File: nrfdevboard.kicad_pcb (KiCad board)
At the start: 4 copper layers, 26 x 26.2 mm, 17 parts, among them J1 Conn_01x07_Pin, J2 Conn_01x07_Pin, P1 USB_C_Plug_USB2.0, U1 MDBT50Q-P1MV2, U3 AP2112K-3.3TRG1, Y1 O_32.768kHz

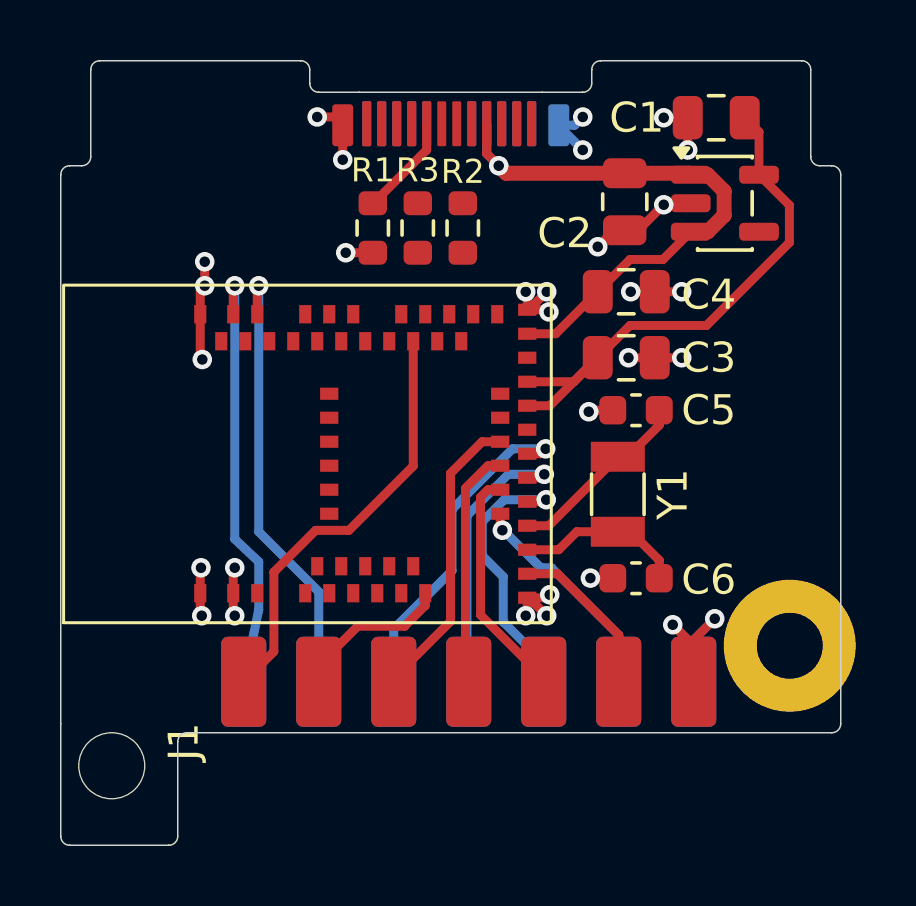
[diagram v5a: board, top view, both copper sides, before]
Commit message: Routing done (outside USB) + added some more pins
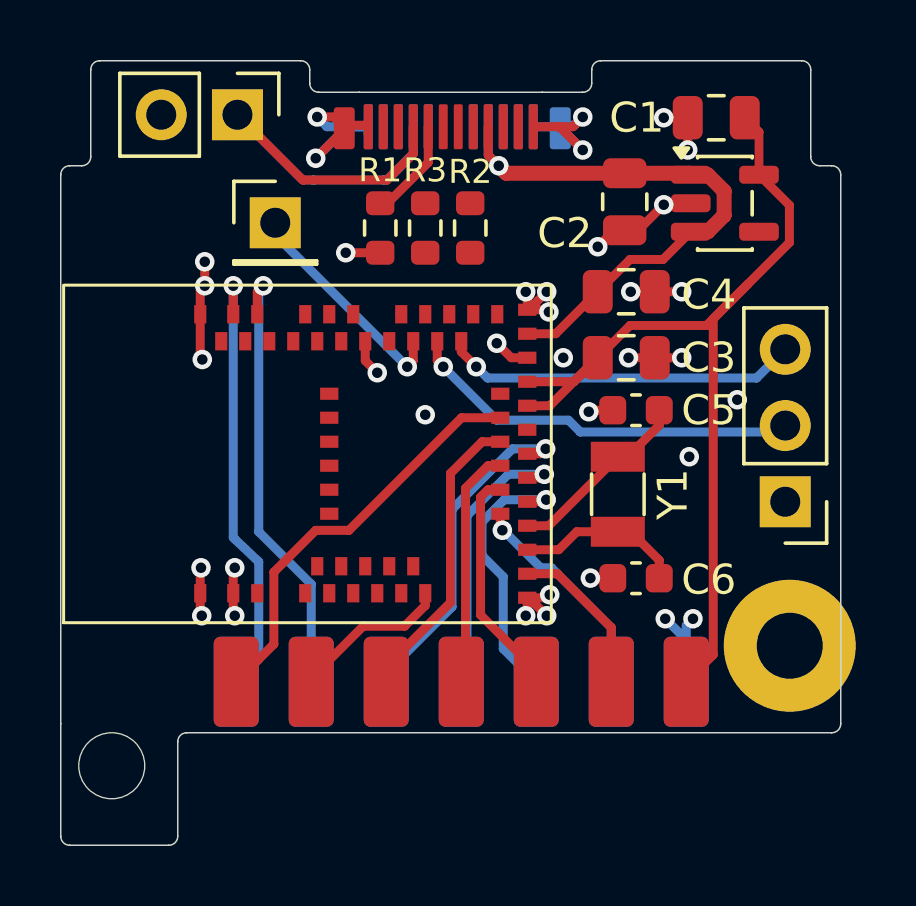
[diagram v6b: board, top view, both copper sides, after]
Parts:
- added J3: 3_tht_side, Connector_PinHeader_2.54mm:PinHeader_1x03_P2.54mm_Vertical, F.Cu at (107.2, 125.7)
- added J4: 2_tht_top, Connector_PinHeader_2.54mm:PinHeader_1x02_P2.54mm_Vertical, F.Cu at (88.9, 112.8)
- added J5: 1_tht_top, Connector_PinHeader_2.54mm:PinHeader_1x01_P2.54mm_Vertical, F.Cu at (90.2, 116.4)
- J1: value Conn_01x07_Pin -> 7_print_front
- J2: value Conn_01x07_Pin -> 7_pin_back
- P1: value USB_C_Plug_USB2.0 -> Straddle_USB_type_c; footprint TH-1-CC:USBC -> TH-1-CC_footprints:USBC
- moved J1 0.25 mm to (87.4, 133.7)
- moved J2 0.25 mm to (87.4, 129.7)
- moved R1 0.25 mm to (93.7, 116.6)
- moved R2 0.25 mm to (96.7, 116.6)
- moved R3 0.25 mm to (95.2, 116.6)
- moved P1 0.11 mm to (92.0, 112.5)
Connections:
- J1 pad 7: GND -> +3.3V
- P1 pad A10: (no net) -> unconnected-(P1-RX2--PadA10)
- P1 pad A11: (no net) -> unconnected-(P1-RX2+-PadA11)
- P1 pad A2: (no net) -> unconnected-(P1-TX1+-PadA2)
- P1 pad A3: (no net) -> unconnected-(P1-TX1--PadA3)
- P1 pad A8: (no net) -> unconnected-(P1-SBU1-PadA8)
- P1 pad B10: (no net) -> unconnected-(P1-RX1--PadB10)
- P1 pad B11: (no net) -> unconnected-(P1-RX1+-PadB11)
- P1 pad B2: (no net) -> unconnected-(P1-TX2+-PadB2)
- P1 pad B3: (no net) -> unconnected-(P1-TX2--PadB3)
- P1 pad B8: (no net) -> unconnected-(P1-SBU2-PadB8)
- U1 pad 27: unconnected-(U1A-P0.11/TRACEDATA2-Pad27) -> PIN8
- U1 pad 36: unconnected-(U1A-P0.14-Pad36) -> PIN15
- U1 pad 38: unconnected-(U1A-P0.16-Pad38) -> PIN16
- U1 pad 40: PIN8 -> PIN20
- U1 pad 43: unconnected-(U1A-P0.21-Pad43) -> PIN17
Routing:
- net PIN17: track 0.00 -> 16.6 mm, vias 0 -> 1
- net VBUS: track 20.0 -> 35.8 mm
- net +3.3V: track 18.5 -> 33.7 mm
- net PIN16: track 0.00 -> 13.3 mm, vias 0 -> 1
- net PIN15: track 0.00 -> 11.9 mm, vias 0 -> 1
- net PIN20: track 0.00 -> 7.56 mm, vias 0 -> 1
- net GND: track 36.1 -> 42.2 mm, vias 30 -> 34
- net unconnected-(U1B-DCCH-Pad31): track 0.00 -> 1.22 mm, vias 0 -> 1
- net PIN9: track 5.33 -> 5.88 mm
- net PIN5: track 9.29 -> 9.83 mm
- added copper zone on In2.Cu, net GND

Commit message: Basics done. Will need to optimise double check DFM before manufacturing
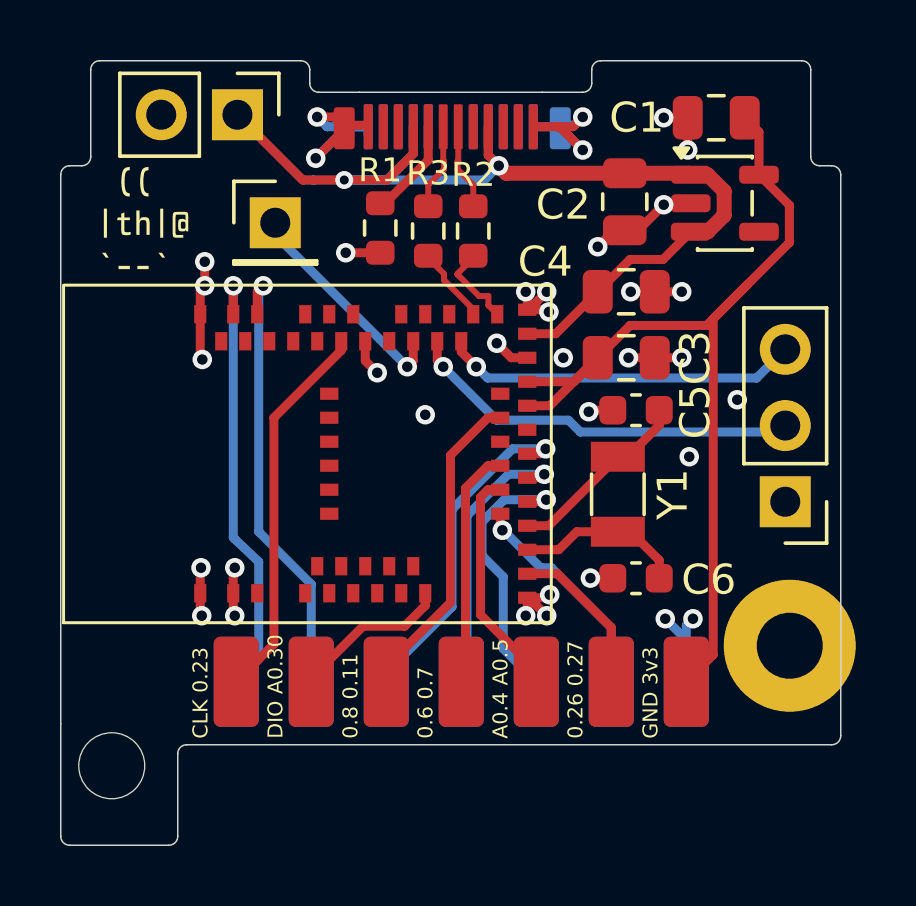
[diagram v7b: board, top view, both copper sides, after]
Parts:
- moved R2 0.14 mm to (96.8, 116.7)
- moved R3 0.14 mm to (95.3, 116.7)
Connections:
- net /D+_r renamed /mcu_D+
- net /D-_r renamed /mcu_D-
- U1 pad 25: PIN10 -> unconnected-(U1A-P1.08-Pad25)
- U1 pad 27: PIN8 -> PIN10
- U1 pad 45: unconnected-(U1A-PO23-Pad45) -> PIN8
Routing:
- net VBUS: track 35.8 -> 41.2 mm, vias 1 -> 2
- net /mcu_D-: track 0.00 -> 2.90 mm
- net D+: track 0.00 -> 2.88 mm
- net D-: track 0.00 -> 2.88 mm
- net /mcu_D+: track 0.00 -> 2.57 mm
- net PIN8: track 13.9 -> 12.8 mm
- net PIN10: track 10.0 -> 10.7 mm
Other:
- outline, holes or cut-outs redrawn
- board text added: "0.26 0.27"
- board text added: "0.6 0.7"
- board text added: "0.8 0.11"
- board text added: "A0.4 A0.5"
- board text added: "CLK 0.23"
- board text added: "DIO A0.30"
- board text added: "GND 3v3"

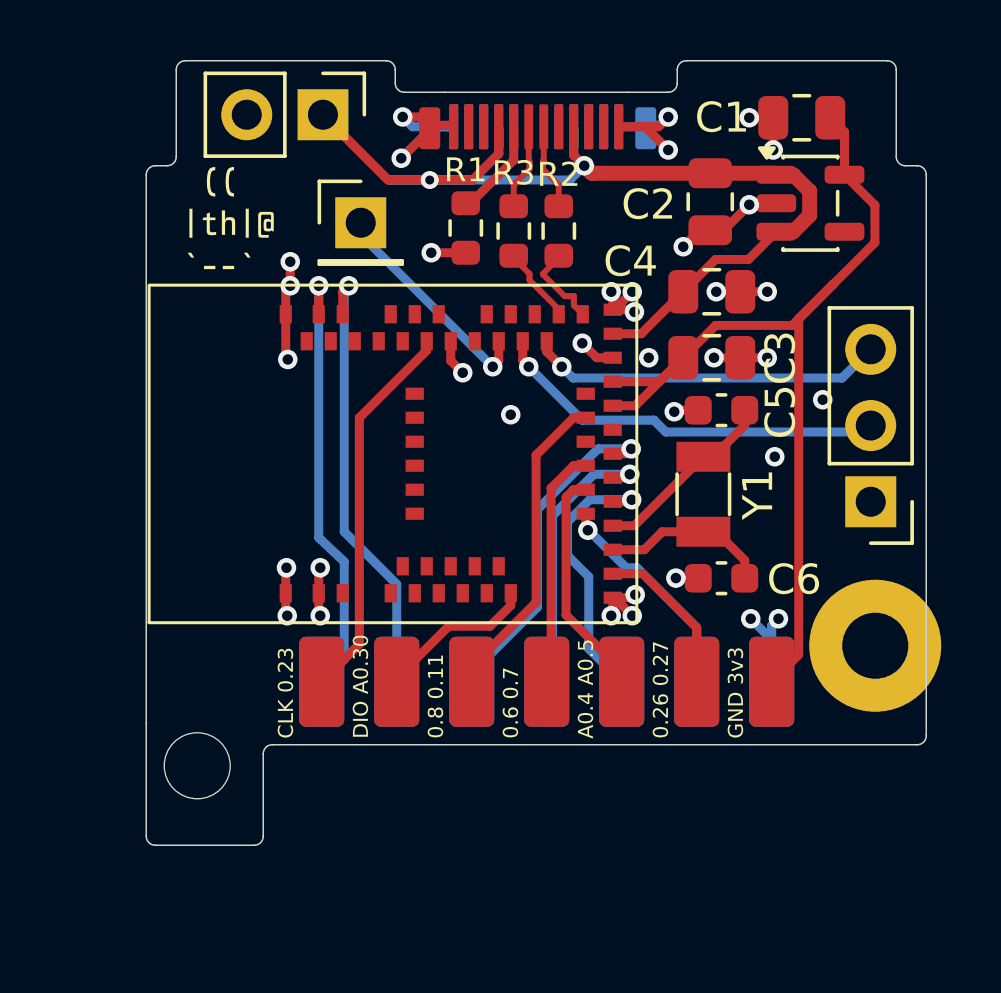
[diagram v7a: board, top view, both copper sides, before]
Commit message: Clearing up DRC errors (part 1)
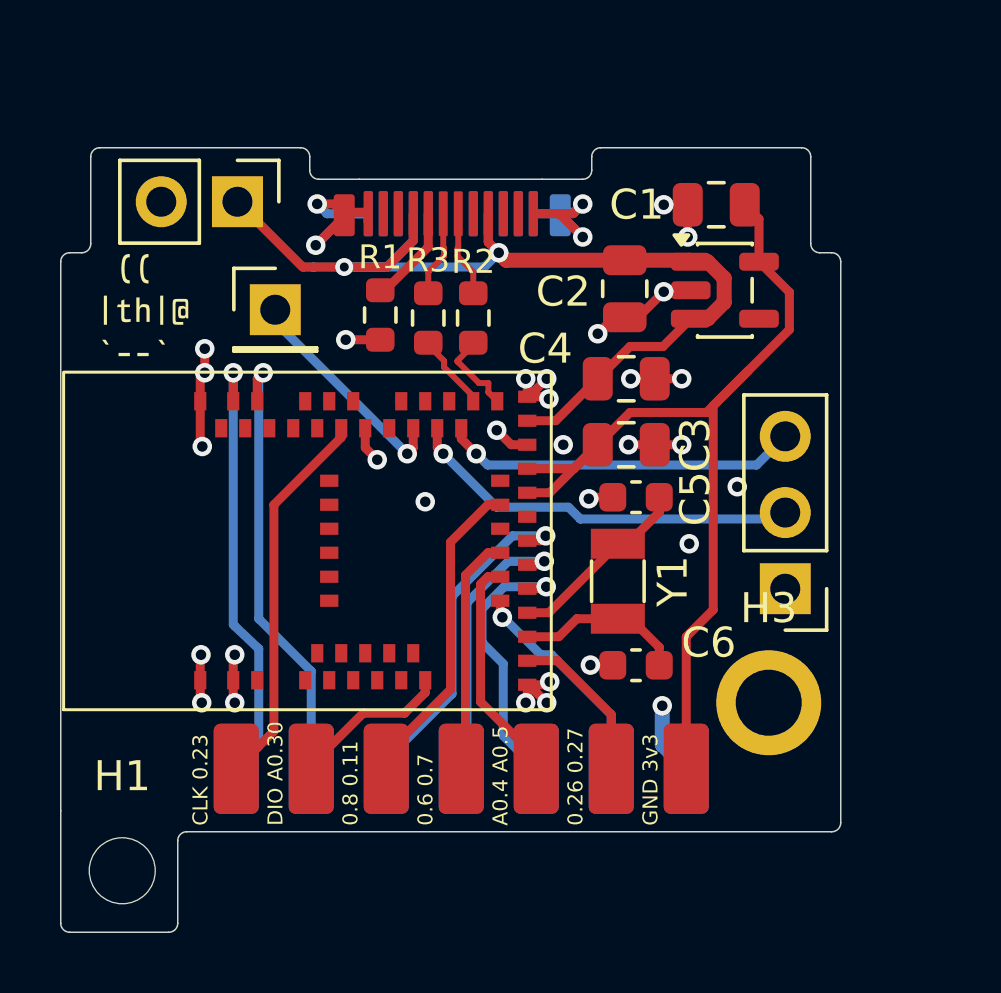
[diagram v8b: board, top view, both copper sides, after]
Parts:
- H1: footprint MountingHole:MountingHole_2.2mm_M2 -> TH-1-CC:PDB_MountingHole_left_2.2mm_M2
- H3: footprint MountingHole:MountingHole_2.2mm_M2_Pad -> TH-1-CC:PDB_MountingHole_right_2.2mm_M2_Pad
- moved H1 4.30 mm to (82.2, 138.0)
- moved J1 4.07 mm to (84.5, 136.6)
- moved J2 4.07 mm to (84.5, 132.6)
- moved C1 4.07 mm to (102.0, 115.8)
- moved C3 4.07 mm to (99.0, 123.8)
- moved C4 4.07 mm to (99.0, 121.6)
- moved C6 4.07 mm to (99.4, 131.2)
- moved J3 4.07 mm to (104.3, 128.6)
- moved J4 4.07 mm to (86.1, 115.7)
- moved J5 4.07 mm to (87.3, 119.3)
- moved R1 4.07 mm to (90.8, 119.5)
- moved R2 4.07 mm to (94.0, 119.6)
- moved R3 4.07 mm to (92.5, 119.6)
- moved U1 4.07 mm to (80.2, 132.8)
- moved U3 4.07 mm to (102.3, 118.7)
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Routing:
- net GND: track 42.2 -> 41.4 mm, vias 34 -> 33
